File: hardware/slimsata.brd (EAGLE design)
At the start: 20.3 x 54.6 mm, 2 parts, among them CON1 MOLEX_67492

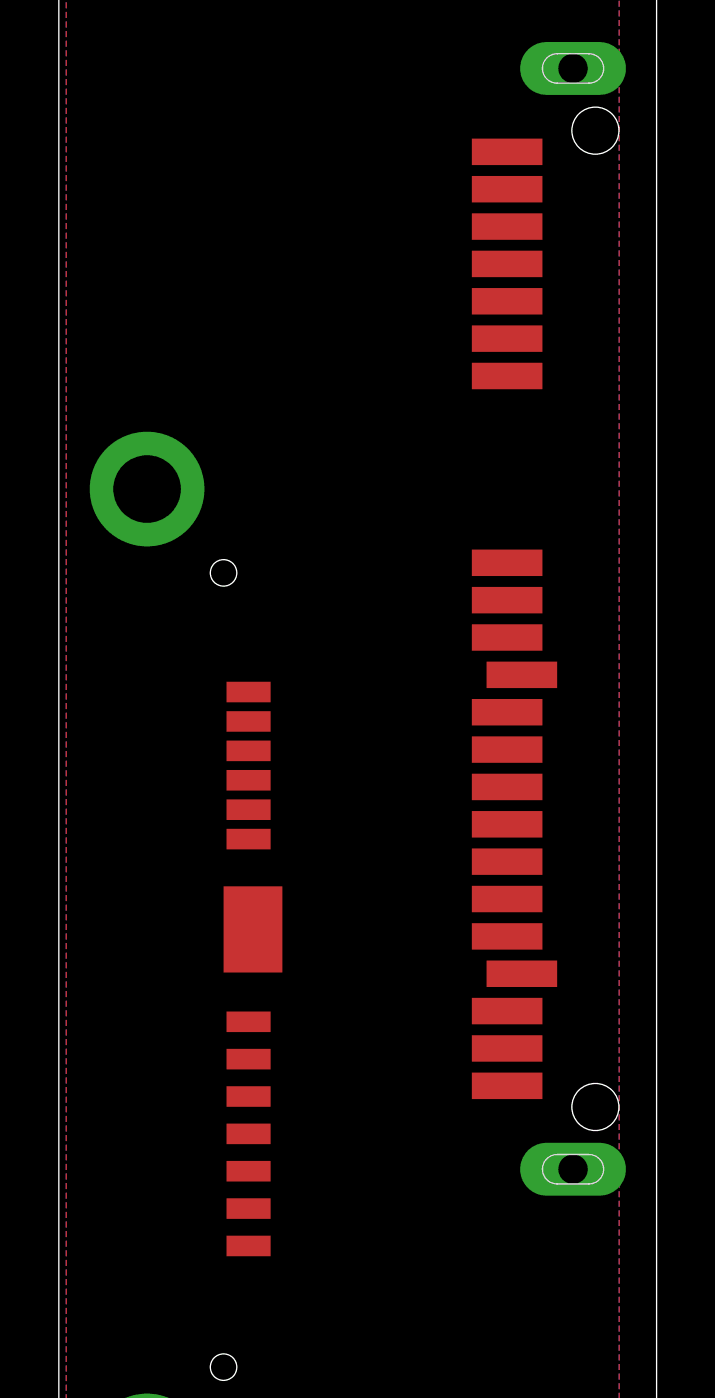
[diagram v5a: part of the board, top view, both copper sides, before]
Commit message: Datenleitungen mit einer Impedanz von 100 Ohm geroutet
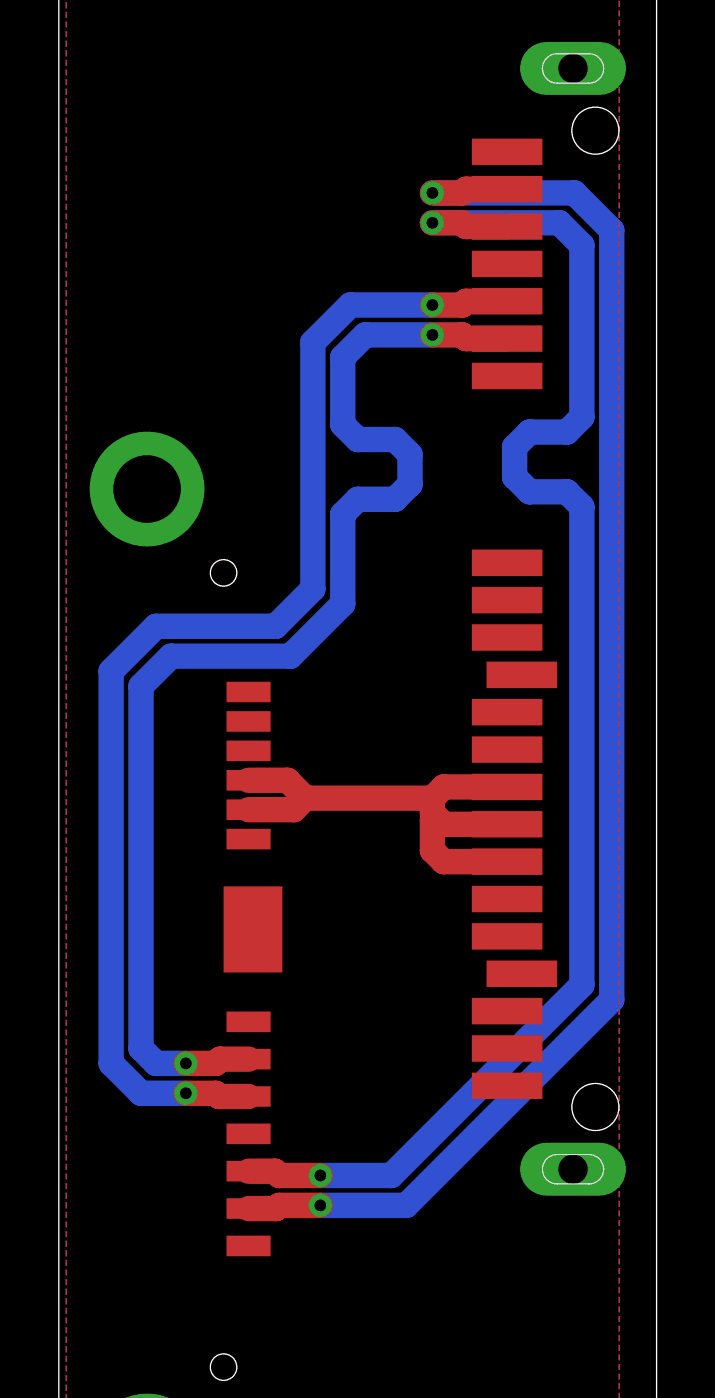
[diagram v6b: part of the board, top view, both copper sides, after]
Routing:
- net N$5: track 0.00 -> 50.7 mm, vias 0 -> 2
- net N$6: track 0.00 -> 50.6 mm, vias 0 -> 2
- net N$7: track 0.00 -> 42.1 mm, vias 0 -> 2
- net N$8: track 0.00 -> 42.0 mm, vias 0 -> 2
- net N$3: track 0.00 -> 18.4 mm
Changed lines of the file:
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@@
 <contactref element="CON1" pad="S2"/>
 <contactref element="CON2" pad="S2"/>
-<wire x1="6.45" y1="12.972" x2="15.24" y2="47.625" width="0" layer="19" extent="1-1"/>
+<wire x1="15.24" y1="47.625" x2="13.843" y2="47.625" width="0.8636" layer="1"/>
+<wire x1="13.843" y1="47.625" x2="13.716" y2="47.498" width="0.8636" layer="1"/>
+<wire x1="13.716" y1="47.498" x2="12.7" y2="47.498" width="0.8636" layer="1"/>
+<via x="12.7" y="47.498" extent="1-16" drill="0.4"/>
+<wire x1="12.7" y1="47.498" x2="17.526" y2="47.498" width="0.8636" layer="16"/>
+<wire x1="17.526" y1="47.498" x2="18.796" y2="46.228" width="0.8636" layer="16"/>
+<wire x1="18.796" y1="20.066" x2="18.796" y2="46.228" width="0.8636" layer="16"/>
+<wire x1="18.796" y1="20.066" x2="11.811" y2="13.081" width="0.8636" layer="16"/>
+<wire x1="11.811" y1="13.081" x2="8.89" y2="13.081" width="0.8636" layer="16"/>
+<via x="8.89" y="13.081" extent="1-16" drill="0.4"/>
+<wire x1="6.45" y1="12.972" x2="7.384" y2="12.972" width="0.8636" layer="1"/>
+<wire x1="7.384" y1="12.972" x2="7.493" y2="13.081" width="0.8636" layer="1"/>
+<wire x1="7.493" y1="13.081" x2="8.89" y2="13.081" width="0.8636" layer="1"/>
 </signal>
 <signal name="N$6">
 <contactref element="CON1" pad="S3"/>
 <contactref element="CON2" pad="S3"/>
-<wire x1="6.45" y1="14.242" x2="15.24" y2="46.355" width="0" layer="19" extent="1-1"/>
+<wire x1="15.24" y1="46.355" x2="13.843" y2="46.355" width="0.8636" layer="1"/>
+<wire x1="13.843" y1="46.355" x2="13.716" y2="46.482" width="0.8636" layer="1"/>
+<wire x1="13.716" y1="46.482" x2="12.7" y2="46.482" width="0.8636" layer="1"/>
+<via x="12.7" y="46.482" extent="1-16" drill="0.4"/>
+<wire x1="12.7" y1="46.482" x2="17.018" y2="46.482" width="0.8636" layer="16"/>
+<wire x1="17.018" y1="46.482" x2="17.78" y2="45.72" width="0.8636" layer="16"/>
+<wire x1="17.78" y1="45.72" x2="17.78" y2="39.878" width="0.8636" layer="16"/>
+<wire x1="17.78" y1="39.878" x2="17.272" y2="39.37" width="0.8636" layer="16"/>
+<wire x1="17.272" y1="39.37" x2="16.002" y2="39.37" width="0.8636" layer="16"/>
+<wire x1="16.002" y1="39.37" x2="15.494" y2="38.862" width="0.8636" layer="16"/>
+<wire x1="15.494" y1="38.862" x2="15.494" y2="37.846" width="0.8636" layer="16"/>
+<wire x1="15.494" y1="37.846" x2="16.002" y2="37.338" width="0.8636" layer="16"/>
+<wire x1="16.002" y1="37.338" x2="17.272" y2="37.338" width="0.8636" layer="16"/>
+<wire x1="17.272" y1="37.338" x2="17.78" y2="36.83" width="0.8636" layer="16"/>
+<wire x1="17.78" y1="36.83" x2="17.78" y2="20.574" width="0.8636" layer="16"/>
+<wire x1="17.78" y1="20.574" x2="11.303" y2="14.097" width="0.8636" layer="16"/>
+<wire x1="11.303" y1="14.097" x2="8.89" y2="14.097" width="0.8636" layer="16"/>
+<via x="8.89" y="14.097" extent="1-16" drill="0.4"/>
+<wire x1="6.45" y1="14.242" x2="7.348" y2="14.242" width="0.8636" layer="1"/>
+<wire x1="7.348" y1="14.242" x2="7.493" y2="14.097" width="0.8636" layer="1"/>
+<wire x1="7.493" y1="14.097" x2="8.89" y2="14.097" width="0.8636" layer="1"/>
 </signal>
 <signal name="N$7">
 <contactref element="CON1" pad="S5"/>
 <contactref element="CON2" pad="S5"/>
-<wire x1="6.45" y1="16.782" x2="15.24" y2="43.815" width="0" layer="19" extent="1-1"/>
+<wire x1="15.24" y1="43.815" x2="13.843" y2="43.815" width="0.8636" layer="1"/>
+<wire x1="13.843" y1="43.815" x2="13.716" y2="43.688" width="0.8636" layer="1"/>
+<wire x1="13.716" y1="43.688" x2="12.7" y2="43.688" width="0.8636" layer="1"/>
+<via x="12.7" y="43.688" extent="1-16" drill="0.4"/>
+<wire x1="12.7" y1="43.688" x2="9.906" y2="43.688" width="0.8636" layer="16"/>
+<wire x1="9.906" y1="43.688" x2="8.636" y2="42.418" width="0.8636" layer="16"/>
+<wire x1="8.636" y1="34.036" x2="8.636" y2="42.418" width="0.8636" layer="16"/>
+<wire x1="8.636" y1="34.036" x2="7.366" y2="32.766" width="0.8636" layer="16"/>
+<wire x1="7.366" y1="32.766" x2="3.302" y2="32.766" width="0.8636" layer="16"/>
+<wire x1="3.302" y1="32.766" x2="1.778" y2="31.242" width="0.8636" layer="16"/>
+<wire x1="1.778" y1="31.242" x2="1.778" y2="17.907" width="0.8636" layer="16"/>
+<wire x1="1.778" y1="17.907" x2="2.794" y2="16.891" width="0.8636" layer="16"/>
+<wire x1="2.794" y1="16.891" x2="4.318" y2="16.891" width="0.8636" layer="16"/>
+<via x="4.318" y="16.891" extent="1-16" drill="0.4"/>
+<wire x1="6.45" y1="16.782" x2="5.443" y2="16.782" width="0.8636" layer="1"/>
+<wire x1="5.443" y1="16.782" x2="5.334" y2="16.891" width="0.8636" layer="1"/>
+<wire x1="5.334" y1="16.891" x2="4.318" y2="16.891" width="0.8636" layer="1"/>
 </signal>
 <signal name="N$8">
 <contactref element="CON1" pad="S6"/>
 <contactref element="CON2" pad="S6"/>
-<wire x1="6.45" y1="18.052" x2="15.24" y2="42.545" width="0" layer="19" extent="1-1"/>
+<wire x1="15.24" y1="42.545" x2="13.843" y2="42.545" width="0.8636" layer="1"/>
+<wire x1="13.843" y1="42.545" x2="13.716" y2="42.672" width="0.8636" layer="1"/>
+<wire x1="13.716" y1="42.672" x2="12.7" y2="42.672" width="0.8636" layer="1"/>
+<via x="12.7" y="42.672" extent="1-16" drill="0.4"/>
+<wire x1="12.7" y1="42.672" x2="10.414" y2="42.672" width="0.8636" layer="16"/>
+<wire x1="10.414" y1="42.672" x2="9.652" y2="41.91" width="0.8636" layer="16"/>
+<wire x1="9.652" y1="41.91" x2="9.652" y2="39.624" width="0.8636" layer="16"/>
+<wire x1="9.652" y1="39.624" x2="10.16" y2="39.116" width="0.8636" layer="16"/>
+<wire x1="10.16" y1="39.116" x2="11.43" y2="39.116" width="0.8636" layer="16"/>
+<wire x1="11.43" y1="39.116" x2="11.938" y2="38.608" width="0.8636" layer="16"/>
+<wire x1="11.938" y1="37.592" x2="11.938" y2="38.608" width="0.8636" layer="16"/>
+<wire x1="11.938" y1="37.592" x2="11.43" y2="37.084" width="0.8636" layer="16"/>
+<wire x1="11.43" y1="37.084" x2="10.16" y2="37.084" width="0.8636" layer="16"/>
+<wire x1="10.16" y1="37.084" x2="9.652" y2="36.576" width="0.8636" layer="16"/>
+<wire x1="9.652" y1="36.576" x2="9.652" y2="33.528" width="0.8636" layer="16"/>
+<wire x1="9.652" y1="33.528" x2="7.874" y2="31.75" width="0.8636" layer="16"/>
+<wire x1="7.874" y1="31.75" x2="3.81" y2="31.75" width="0.8636" layer="16"/>
+<wire x1="3.81" y1="31.75" x2="2.794" y2="30.734" width="0.8636" layer="16"/>
+<wire x1="2.794" y1="30.734" x2="2.794" y2="18.415" width="0.8636" layer="16"/>
+<wire x1="3.302" y1="17.907" x2="2.794" y2="18.415" width="0.8636" layer="16"/>
+<wire x1="3.302" y1="17.907" x2="4.318" y2="17.907" width="0.8636" layer="16"/>
+<via x="4.318" y="17.907" extent="1-16" drill="0.4"/>
+<wire x1="6.45" y1="18.052" x2="5.479" y2="18.052" width="0.8636" layer="1"/>
+<wire x1="5.479" y1="18.052" x2="5.334" y2="17.907" width="0.8636" layer="1"/>
+<wire x1="5.334" y1="17.907" x2="4.318" y2="17.907" width="0.8636" layer="1"/>
 </signal>
 <signal name="N$3">
@@
 <contactref element="CON2" pad="P2"/>
 <contactref element="CON2" pad="P3"/>
-<wire x1="15.24" y1="26.035" x2="15.24" y2="27.305" width="0" layer="19" extent="1-1"/>
-<wire x1="15.24" y1="24.765" x2="15.24" y2="26.035" width="0" layer="19" extent="1-1"/>
-<wire x1="6.45" y1="27.532" x2="6.45" y2="26.532" width="0" layer="19" extent="1-1"/>
-<wire x1="6.45" y1="26.532" x2="15.24" y2="26.035" width="0" layer="19" extent="1-1"/>
+<wire x1="6.45" y1="26.532" x2="7.99" y2="26.532" width="0.8636" layer="1"/>
+<wire x1="7.99" y1="26.532" x2="8.382" y2="26.924" width="0.8636" layer="1"/>
+<wire x1="6.45" y1="27.532" x2="7.774" y2="27.532" width="0.8636" layer="1"/>
+<wire x1="15.24" y1="27.305" x2="13.081" y2="27.305" width="0.8636" layer="1"/>
+<wire x1="13.081" y1="27.305" x2="12.7" y2="26.924" width="0.8636" layer="1"/>
+<wire x1="12.7" y1="26.924" x2="8.382" y2="26.924" width="0.8636" layer="1"/>
+<wire x1="7.774" y1="27.532" x2="8.382" y2="26.924" width="0.8636" layer="1"/>
+<wire x1="15.24" y1="26.035" x2="13.081" y2="26.035" width="0.8636" layer="1"/>
+<wire x1="13.081" y1="26.035" x2="12.827" y2="26.289" width="0.8636" layer="1"/>
+<wire x1="12.827" y1="26.289" x2="12.7" y2="26.416" width="0.8636" layer="1"/>
+<wire x1="12.7" y1="26.416" x2="12.7" y2="26.924" width="0.8636" layer="1"/>
+<wire x1="15.24" y1="24.765" x2="13.081" y2="24.765" width="0.8636" layer="1"/>
+<wire x1="13.081" y1="24.765" x2="12.7" y2="25.146" width="0.8636" layer="1"/>
+<wire x1="12.7" y1="25.146" x2="12.7" y2="26.162" width="0.8636" layer="1"/>
+<wire x1="12.7" y1="26.162" x2="12.827" y2="26.289" width="0.8636" layer="1"/>
 </signal>
 <signal name="GND">
@@
 <vertex x="0.254" y="0.254"/>
 </polygon>
-<wire x1="15.24" y1="48.895" x2="17.48" y2="51.73" width="0" layer="19" extent="1-1"/>
-<wire x1="15.24" y1="45.085" x2="15.24" y2="48.895" width="0" layer="19" extent="1-1"/>
-<wire x1="15.24" y1="41.275" x2="15.24" y2="45.085" width="0" layer="19" extent="1-1"/>
-<wire x1="15.74" y1="31.115" x2="15.24" y2="41.275" width="0" layer="19" extent="1-1"/>
-<wire x1="15.24" y1="29.845" x2="15.74" y2="31.115" width="0" layer="19" extent="1-1"/>
-<wire x1="15.24" y1="28.575" x2="15.24" y2="29.845" width="0" layer="19" extent="1-1"/>
-<wire x1="15.24" y1="23.495" x2="15.24" y2="28.575" width="0" layer="19" extent="1-1"/>
-<wire x1="15.74" y1="20.955" x2="15.24" y2="23.495" width="0" layer="19" extent="1-1"/>
-<wire x1="17.48" y1="14.31" x2="15.74" y2="20.955" width="0" layer="19" extent="1-1"/>
-<wire x1="6.6" y1="22.462" x2="15.24" y2="23.495" width="0" layer="19" extent="1-1"/>
-<wire x1="6.45" y1="19.322" x2="6.6" y2="22.462" width="0" layer="19" extent="1-1"/>
-<wire x1="6.45" y1="15.512" x2="6.45" y2="19.322" width="0" layer="19" extent="1-1"/>
-<wire x1="6.45" y1="11.702" x2="6.45" y2="15.512" width="0" layer="19" extent="1-1"/>
-<wire x1="6.45" y1="29.532" x2="6.6" y2="22.462" width="0" layer="19" extent="1-1"/>
-<wire x1="6.45" y1="30.532" x2="6.45" y2="29.532" width="0" layer="19" extent="1-1"/>
-<wire x1="3" y1="37.432" x2="6.45" y2="30.532" width="0" layer="19" extent="1-1"/>
-<wire x1="3" y1="4.732" x2="6.45" y2="11.702" width="0" layer="19" extent="1-1"/>
 </signal>
 </signals>
